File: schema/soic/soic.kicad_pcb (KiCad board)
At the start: 2 copper layers, 33.7 x 13 mm, 5 parts, among them J1 Conn_01x04_Male, J2 Conn_01x04_Male, U1 LF398_SOIC8

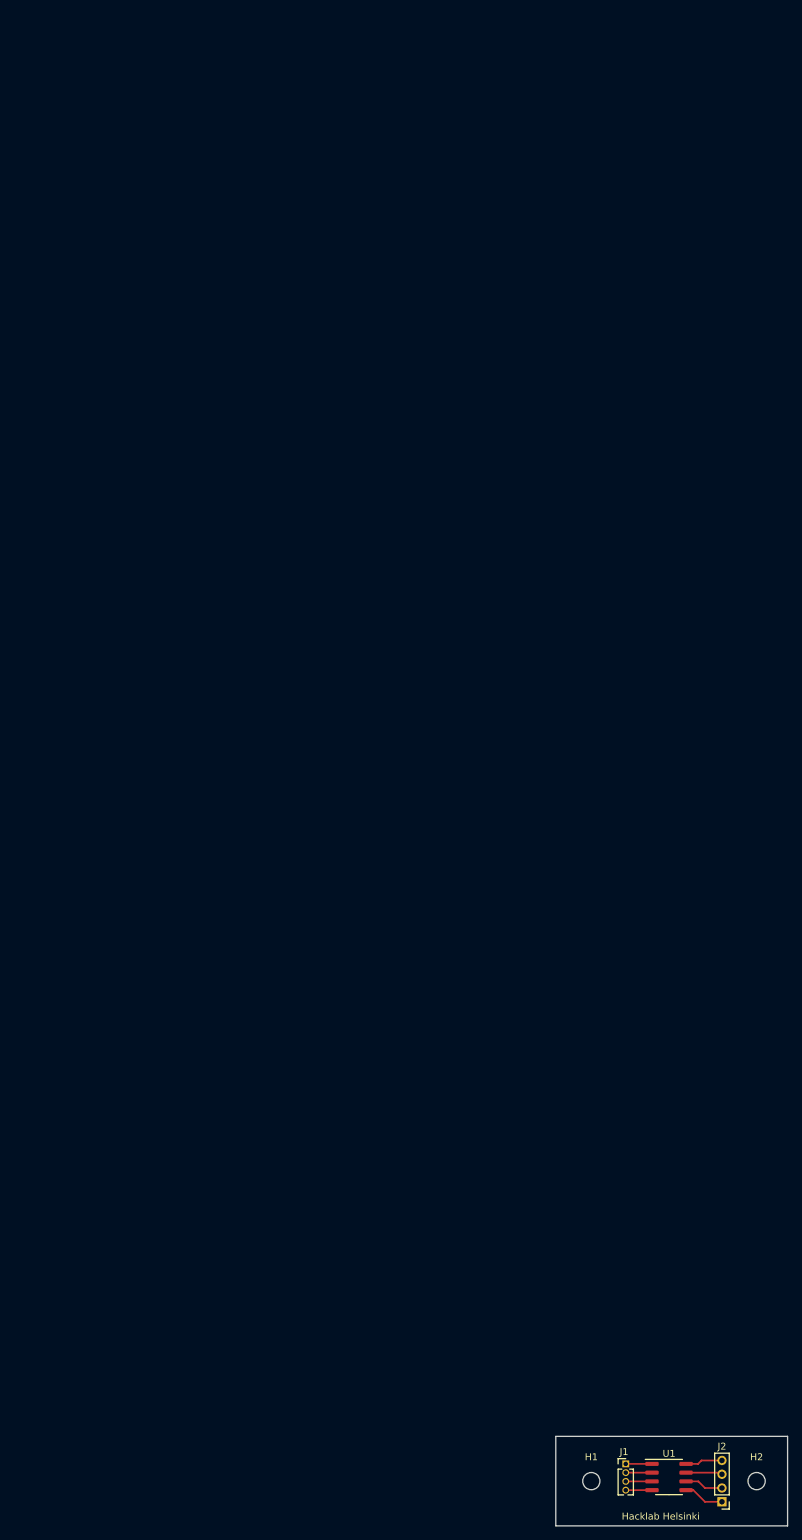
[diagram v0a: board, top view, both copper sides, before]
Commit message: installation instruction, 1/2 sided PCB instructions
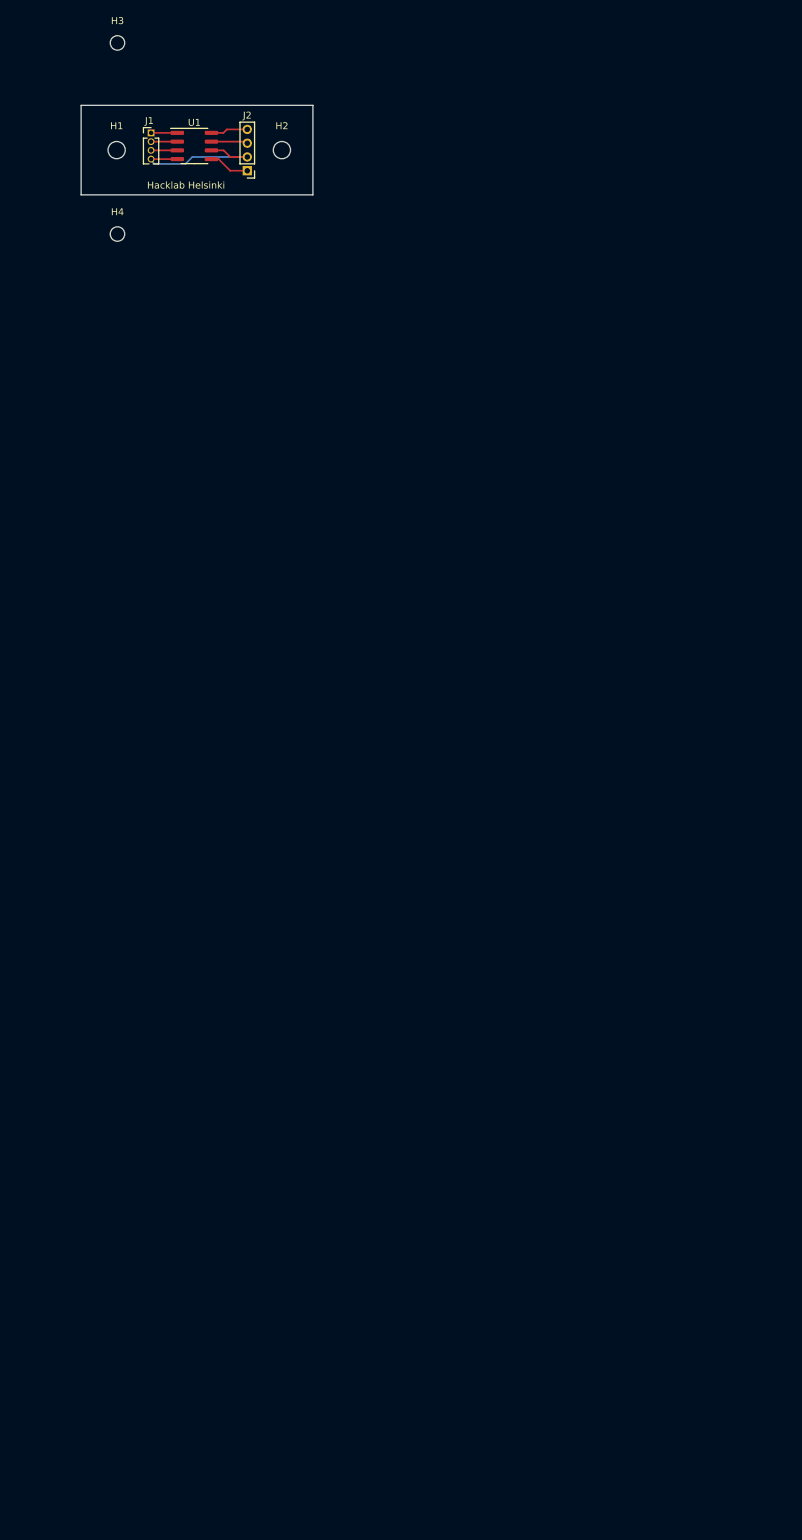
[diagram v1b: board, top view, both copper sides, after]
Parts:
- added H3: MountingHole, MountingHole:MountingHole_2.1mm, F.Cu at (0.00, -27.8)
- added H4: MountingHole, MountingHole:MountingHole_2.1mm, F.Cu at (0.00, -0.00)
- moved H1 205.2 mm to (-0.12, -12.2)
- moved H2 205.2 mm to (23.9, -12.2)
- moved J1 205.2 mm to (4.88, -14.7)
- moved J2 205.2 mm to (18.9, -9.19)
- moved U1 205.2 mm to (11.2, -12.8)
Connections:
- J2 pad 2: Net-(J2-Pad2) -> Net-(J1-Pad4)
- U1 pad 6: Net-(J2-Pad2) -> Net-(J1-Pad4)
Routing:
- net Net-(J1-Pad4): track 3.81 -> 24.0 mm
- net Net-(J2-Pad2): track 5.64 -> 0.00 mm
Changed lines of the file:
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@@
     (thickness 1.6)
     (drawings 5)
-    (tracks 14)
+    (tracks 19)
     (zones 0)
-    (modules 5)
-    (nets 9)
+    (modules 7)
+    (nets 8)
   )
   (page A4)
@@
     (pad_drill 0.762)
     (pad_to_mask_clearance 0)
-    (aux_axis_origin 0 0)
-    (grid_origin 3.81 -0.4064)
+    (aux_axis_origin 0 -0.0048)
+    (grid_origin 0 -0.0048)
     (visible_elements FFFFFF7F)
     (pcbplotparams
@@
   (net 5 "Net-(J2-Pad4)")
   (net 6 "Net-(J2-Pad3)")
-  (net 7 "Net-(J2-Pad2)")
-  (net 8 "Net-(J2-Pad1)")
+  (net 7 "Net-(J2-Pad1)")
   (net_class Default "This is the default net class."
     (clearance 0.2)
@@
     (add_net "Net-(J1-Pad4)")
     (add_net "Net-(J2-Pad1)")
-    (add_net "Net-(J2-Pad2)")
     (add_net "Net-(J2-Pad3)")
     (add_net "Net-(J2-Pad4)")
   )
+  (module MountingHole:MountingHole_2.1mm (layer F.Cu)
+    (at 0 -0.0048)
+    (descr "Mounting Hole 2.1mm, no annular")
+    (tags "mounting hole 2.1mm no annular")
+    (attr virtual)
+    (fp_text reference H4 (at 0 -3.2) (layer F.SilkS)
+      (effects (font (size 1 1) (thickness 0.15)))
+    )
+    (fp_text value MountingHole (at 0 3.2) (layer F.Fab)
+      (effects (font (size 1 1) (thickness 0.15)))
+    )
+    (fp_text user %R (at 0.3 0) (layer F.Fab)
+      (effects (font (size 1 1) (thickness 0.15)))
+    )
+    (fp_circle (center 0 0) (end 2.1 0) (layer Cmts.User) (width 0.15))
+    (fp_circle (center 0 0) (end 2.35 0) (layer F.CrtYd) (width 0.05))
+    (pad "" np_thru_hole circle (at 0 0) (size 2.1 2.1) (drill 2.1) (layers *.Cu *.Mask))
+  )
+  (module MountingHole:MountingHole_2.1mm (layer F.Cu)
+    (at 0 -27.7548)
+    (descr "Mounting Hole 2.1mm, no annular")
+    (tags "mounting hole 2.1mm no annular")
+    (attr virtual)
+    (fp_text reference H3 (at 0 -3.2) (layer F.SilkS)
+      (effects (font (size 1 1) (thickness 0.15)))
+    )
+    (fp_text value MountingHole (at 0 3.2) (layer F.Fab)
+      (effects (font (size 1 1) (thickness 0.15)))
+    )
+    (fp_text user %R (at 0.3 0) (layer F.Fab)
+      (effects (font (size 1 1) (thickness 0.15)))
+    )
+    (fp_circle (center 0 0) (end 2.1 0) (layer Cmts.User) (width 0.15))
+    (fp_circle (center 0 0) (end 2.35 0) (layer F.CrtYd) (width 0.05))
+    (pad "" np_thru_hole circle (at 0 0) (size 2.1 2.1) (drill 2.1) (layers *.Cu *.Mask))
+  )
   (module MountingHole:MountingHole_2.5mm (layer F.Cu)
-    (at 92.81 181.0936)
+    (at 23.88 -12.1928)
     (descr "Mounting Hole 2.5mm, no annular")
     (tags "mounting hole 2.5mm no annular")
@@
       (effects (font (size 1 1) (thickness 0.15)))
     )
-    (fp_text user %R (at 0.3 0) (layer F.Fab)
-      (effects (font (size 1 1) (thickness 0.15)))
-    )
     (fp_circle (center 0 0) (end 2.5 0) (layer Cmts.User) (width 0.15))
     (fp_circle (center 0 0) (end 2.75 0) (layer F.CrtYd) (width 0.05))
+    (fp_text user %R (at 0.3 0) (layer F.Fab)
+      (effects (font (size 1 1) (thickness 0.15)))
+    )
     (pad 1 np_thru_hole circle (at 0 0) (size 2.5 2.5) (drill 2.5) (layers *.Cu *.Mask))
   )
   (module MountingHole:MountingHole_2.5mm (layer F.Cu)
-    (at 68.81 181.0936)
+    (at -0.12 -12.1928)
     (descr "Mounting Hole 2.5mm, no annular")
     (tags "mounting hole 2.5mm no annular")
@@
       (effects (font (size 1 1) (thickness 0.15)))
     )
-    (fp_text user %R (at 0.3 0) (layer F.Fab)
-      (effects (font (size 1 1) (thickness 0.15)))
-    )
     (fp_circle (center 0 0) (end 2.5 0) (layer Cmts.User) (width 0.15))
     (fp_circle (center 0 0) (end 2.75 0) (layer F.CrtYd) (width 0.05))
+    (fp_text user %R (at 0.3 0) (layer F.Fab)
+      (effects (font (size 1 1) (thickness 0.15)))
+    )
     (pad 1 np_thru_hole circle (at 0 0) (size 2.5 2.5) (drill 2.5) (layers *.Cu *.Mask))
   )
   (module Connector_PinHeader_2.00mm:PinHeader_1x04_P2.00mm_Vertical (layer F.Cu)
-    (at 87.78 184.0936 180)
+    (at 18.85 -9.1928 180)
     (descr "Through hole straight pin header, 1x04, 2.00mm pitch, single row")
     (tags "Through hole pin header THT 1x04 2.00mm single row")
@@
       (net 6 "Net-(J2-Pad3)"))
     (pad 2 thru_hole oval (at 0 2 180) (size 1.35 1.35) (drill 0.8) (layers *.Cu *.Mask)
-      (net 7 "Net-(J2-Pad2)"))
+      (net 1 "Net-(J1-Pad4)"))
     (pad 1 thru_hole rect (at 0 0 180) (size 1.35 1.35) (drill 0.8) (layers *.Cu *.Mask)
-      (net 8 "Net-(J2-Pad1)"))
+      (net 7 "Net-(J2-Pad1)"))
     (model ${KISYS3DMOD}/Connector_PinHeader_2.00mm.3dshapes/PinHeader_1x04_P2.00mm_Vertical.wrl
       (at (xyz 0 0 0))
@@
   )
   (module Connector_PinHeader_1.27mm:PinHeader_1x04_P1.27mm_Vertical (layer F.Cu)
-    (at 73.81 178.5936)
+    (at 4.88 -14.6928)
     (descr "Through hole straight pin header, 1x04, 1.27mm pitch, single row")
     (tags "Through hole pin header THT 1x04 1.27mm single row")
@@
   )
   (module Package_SO:SOIC-8_3.9x4.9mm_P1.27mm (layer F.Cu)
-    (at 80.095 180.4986)
+    (at 11.165 -12.7878)
     (descr "SOIC, 8 Pin (JEDEC MS-012AA, https://www.analog.com/media/en/package-pcb-resources/package/pkg_pdf/soic_narrow-r/r_8.pdf), generated with kicad-footprint-generator ipc_gullwing_generator.py")
     (tags "SOIC SO")
@@
       (net 6 "Net-(J2-Pad3)"))
     (pad 6 smd roundrect (at 2.475 0.635) (size 1.95 0.6) (layers F.Cu F.Paste F.Mask) (roundrect_rratio 0.25)
-      (net 7 "Net-(J2-Pad2)"))
+      (net 1 "Net-(J1-Pad4)"))
     (pad 5 smd roundrect (at 2.475 1.905) (size 1.95 0.6) (layers F.Cu F.Paste F.Mask) (roundrect_rratio 0.25)
-      (net 8 "Net-(J2-Pad1)"))
+      (net 7 "Net-(J2-Pad1)"))
     (pad 4 smd roundrect (at -2.475 1.905) (size 1.95 0.6) (layers F.Cu F.Paste F.Mask) (roundrect_rratio 0.25)
       (net 1 "Net-(J1-Pad4)"))
@@
     )
   )
-  (gr_text "Hacklab Helsinki" (at 78.89 186.2136) (layer F.SilkS)
+  (gr_text "Hacklab Helsinki" (at 9.96 -7.0728) (layer F.SilkS)
     (effects (font (size 1 1) (thickness 0.15)))
   )
-  (gr_line (start 97.31 174.5936) (end 97.31 187.5936) (layer Edge.Cuts) (width 0.1))
-  (gr_line (start 63.65 174.5936) (end 97.31 174.5936) (layer Edge.Cuts) (width 0.1))
-  (gr_line (start 63.65 187.5936) (end 63.65 174.5936) (layer Edge.Cuts) (width 0.1))
-  (gr_line (start 97.31 187.5936) (end 63.65 187.5936) (layer Edge.Cuts) (width 0.1))
-  (segment (start 73.81 182.4036) (end 77.62 182.4036) (width 0.25) (layer F.Cu) (net 1))
-  (segment (start 73.81 181.1336) (end 77.62 181.1336) (width 0.25) (layer F.Cu) (net 2))
-  (segment (start 73.81 179.8636) (end 77.62 179.8636) (width 0.25) (layer F.Cu) (net 3))
-  (segment (start 73.81 178.5936) (end 77.62 178.5936) (width 0.25) (layer F.Cu) (net 4))
-  (segment (start 82.57 178.5936) (end 84.31 178.5936) (width 0.25) (layer F.Cu) (net 5))
-  (segment (start 84.31 178.5936) (end 84.81 178.0936) (width 0.25) (layer F.Cu) (net 5))
-  (segment (start 84.81 178.0936) (end 87.81 178.0936) (width 0.25) (layer F.Cu) (net 5))
-  (segment (start 82.57 179.8636) (end 87.58 179.8636) (width 0.25) (layer F.Cu) (net 6))
-  (segment (start 82.57 181.1336) (end 84.35 181.1336) (width 0.25) (layer F.Cu) (net 7))
-  (segment (start 84.35 181.1336) (end 85.31 182.0936) (width 0.25) (layer F.Cu) (net 7))
-  (segment (start 85.31 182.0936) (end 87.81 182.0936) (width 0.25) (layer F.Cu) (net 7))
-  (segment (start 82.57 182.4036) (end 83.62 182.4036) (width 0.25) (layer F.Cu) (net 8))
-  (segment (start 83.62 182.4036) (end 85.31 184.0936) (width 0.25) (layer F.Cu) (net 8))
-  (segment (start 85.31 184.0936) (end 87.81 184.0936) (width 0.25) (layer F.Cu) (net 8))
+  (gr_line (start 28.38 -18.6928) (end 28.38 -5.6928) (layer Edge.Cuts) (width 0.1))
+  (gr_line (start -5.28 -18.6928) (end 28.38 -18.6928) (layer Edge.Cuts) (width 0.1))
+  (gr_line (start -5.28 -5.6928) (end -5.28 -18.6928) (layer Edge.Cuts) (width 0.1))
+  (gr_line (start 28.38 -5.6928) (end -5.28 -5.6928) (layer Edge.Cuts) (width 0.1))
+  (segment (start 4.88 -10.8828) (end 8.69 -10.8828) (width 0.25) (layer F.Cu) (net 1))
+  (segment (start 13.64 -12.1528) (end 15.42 -12.1528) (width 0.25) (layer F.Cu) (net 1))
+  (segment (start 15.42 -12.1528) (end 16.38 -11.1928) (width 0.25) (layer F.Cu) (net 1))
+  (segment (start 16.38 -11.1928) (end 18.88 -11.1928) (width 0.25) (layer F.Cu) (net 1))
+  (segment (start 18.85 -11.1928) (end 10.88 -11.1928) (width 0.25) (layer B.Cu) (net 1))
+  (segment (start 10.88 -11.1928) (end 9.88 -10.1928) (width 0.25) (layer B.Cu) (net 1))
+  (segment (start 9.88 -10.1928) (end 5.88 -10.1928) (width 0.25) (layer B.Cu) (net 1))
+  (segment (start 5.88 -10.1928) (end 5.38 -10.1928) (width 0.25) (layer B.Cu) (net 1))
+  (segment (start 5.38 -10.1928) (end 4.88 -10.6928) (width 0.25) (layer B.Cu) (net 1))
+  (segment (start 4.88 -12.1528) (end 8.69 -12.1528) (width 0.25) (layer F.Cu) (net 2))
+  (segment (start 4.88 -13.4228) (end 8.69 -13.4228) (width 0.25) (layer F.Cu) (net 3))
+  (segment (start 4.88 -14.6928) (end 8.69 -14.6928) (width 0.25) (layer F.Cu) (net 4))
+  (segment (start 13.64 -14.6928) (end 15.38 -14.6928) (width 0.25) (layer F.Cu) (net 5))
+  (segment (start 15.38 -14.6928) (end 15.88 -15.1928) (width 0.25) (layer F.Cu) (net 5))
+  (segment (start 15.88 -15.1928) (end 18.88 -15.1928) (width 0.25) (layer F.Cu) (net 5))
+  (segment (start 13.64 -13.4228) (end 18.65 -13.4228) (width 0.25) (layer F.Cu) (net 6))
+  (segment (start 13.64 -10.8828) (end 14.69 -10.8828) (width 0.25) (layer F.Cu) (net 7))
+  (segment (start 14.69 -10.8828) (end 16.38 -9.1928) (width 0.25) (layer F.Cu) (net 7))
+  (segment (start 16.38 -9.1928) (end 18.88 -9.1928) (width 0.25) (layer F.Cu) (net 7))
 )

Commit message: prepare for rel 3
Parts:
- moved H3 5.75 mm to (0.00, -22.0)
- moved J1 5.30 mm to (10.1, -13.9)
- moved H1 5.30 mm to (5.13, -11.4)
- moved H2 5.30 mm to (29.1, -11.4)
- moved J2 5.30 mm to (24.1, -8.44)
- moved U1 5.30 mm to (16.4, -12.0)
